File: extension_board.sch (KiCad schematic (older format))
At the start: 37 parts, among them CN1 Conn_02x20_Odd_Even, CN11 Conn_02x05_Odd_Even, CN12 Conn_02x20_Odd_Even, J1 Screw_Terminal_01x02, J2 Conn_01x02, J3 Conn_01x02, J4 Conn_01x02, J5 Conn_02x03_Odd_Even, J6 Conn_01x02, J7 Conn_02x14_Odd_Even, U1 LM334Z, U2 LM334Z, U3 LM334Z, U4 LM334Z

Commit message: first version of the pcb
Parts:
- removed CN11: Conn_02x05_Odd_Even, symbol Connector_Generic:Conn_02x05_Odd_Even
- removed CN12: Conn_02x20_Odd_Even, symbol Connector_Generic:Conn_02x20_Odd_Even
- added J8: Conn_02x10_Odd_Even, Connector_PinHeader_2.54mm:PinHeader_2x10_P2.54mm_Vertical, symbol Connector_Generic:Conn_02x10_Odd_Even
- added J9: Conn_02x19_Odd_Even, Connector_PinHeader_2.54mm:PinHeader_2x19_P2.54mm_Vertical, symbol Connector_Generic:Conn_02x19_Odd_Even
- C1: footprint (none) -> Capacitor_SMD:CP_Elec_4x5.8
- CN1: footprint (none) -> Connector_PinHeader_2.54mm:PinHeader_2x20_P2.54mm_Vertical_SMD
- D1: footprint (none) -> LED_SMD:LED_0805_2012Metric_Pad1.15x1.40mm_HandSolder
- J1: footprint (none) -> digikey-footprints:Term_Block_1x2_P5.08MM
- J2, J3, J4, J6: footprint (none) -> Connector_PinHeader_2.54mm:PinHeader_2x01_P2.54mm_Vertical_SMD
- J5: footprint (none) -> Connector_PinHeader_2.54mm:PinHeader_2x03_P2.54mm_Vertical_SMD
- J7: footprint (none) -> Connector_PinHeader_2.54mm:PinHeader_2x14_P2.54mm_Vertical_SMD
- R1, R2, R3, R4, R5, R6, R7, R8, R9: footprint (none) -> Resistor_SMD:R_0805_2012Metric_Pad1.15x1.40mm_HandSolder
- RV1, RV2, RV3, RV4: footprint (none) -> digikey-footprints:Trimpot_3.8mmx3.6mm_TC33X-2-103E
- TP1, TP2, TP3, TP4: footprint (none) -> TestPoint:TestPoint_Pad_2.5x2.5mm
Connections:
- net labels added: PA15, PF7
- wire segments 111 -> 113
- no-connect marks 55 -> 59

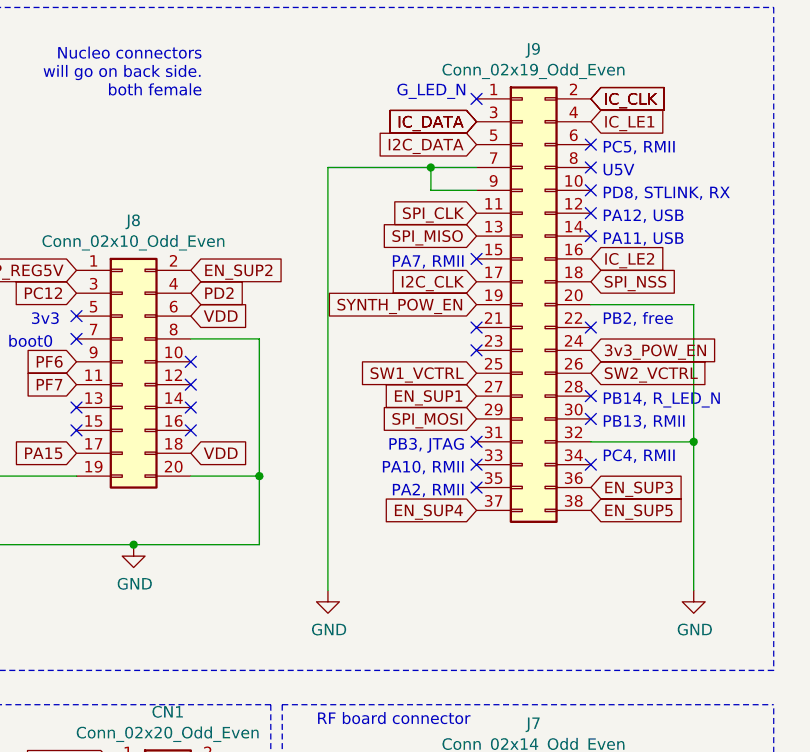
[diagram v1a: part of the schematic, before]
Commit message: had shorted gnd and AVDD on the cn12 connector
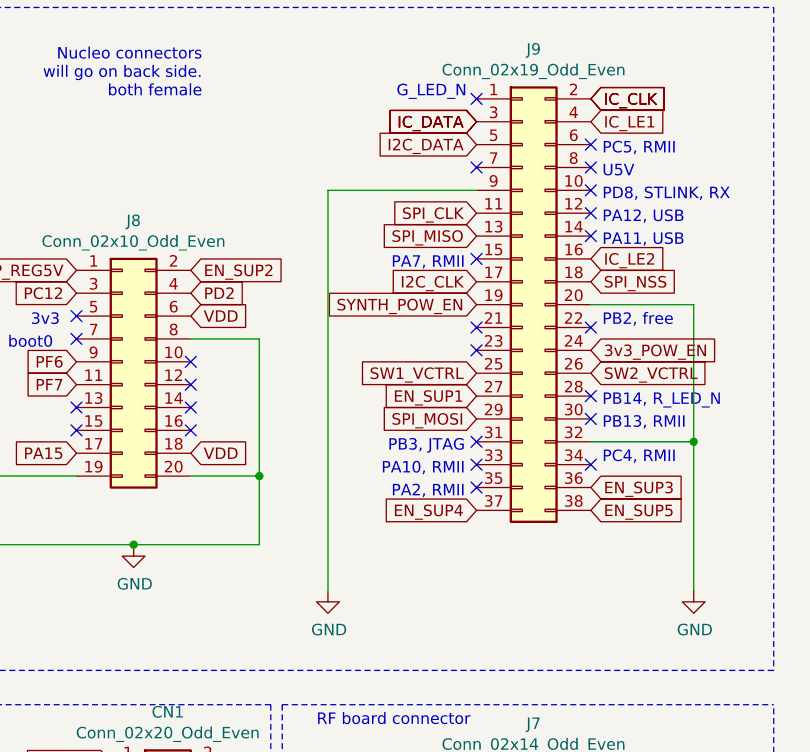
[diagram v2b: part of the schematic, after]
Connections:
- wire segments 113 -> 110
- no-connect marks 59 -> 60
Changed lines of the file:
@@
 Text Notes 7450 7500 0    50   ~ 0
 Glue board to connect to Nucleo, Power board and RF board
-Wire Wire Line
-	9800 1350 9600 1350
-Wire Wire Line
-	9600 1350 9600 1250
 $Comp
 L power:GND #PWR09
@@
 Text GLabel 9800 1850 0    50   Input ~ 0
 SYNTH_POW_EN
-Wire Wire Line
-	9150 1250 9600 1250
-Connection ~ 9600 1250
-Wire Wire Line
-	9600 1250 9800 1250
 Text GLabel 9800 1750 0    50   Input ~ 0
 I2C_CLK
@@
 	1    0    0    -1
 $EndComp
-Wire Wire Line
-	9150 1250 9150 3100
 NoConn ~ 8050 2300
 NoConn ~ 8050 2400
@@
 Wire Wire Line
 	5950 4800 5950 4900
+Wire Wire Line
+	9150 1350 9150 3100
+Wire Wire Line
+	9150 1350 9800 1350
+NoConn ~ 9800 1250
 $EndSCHEMATC

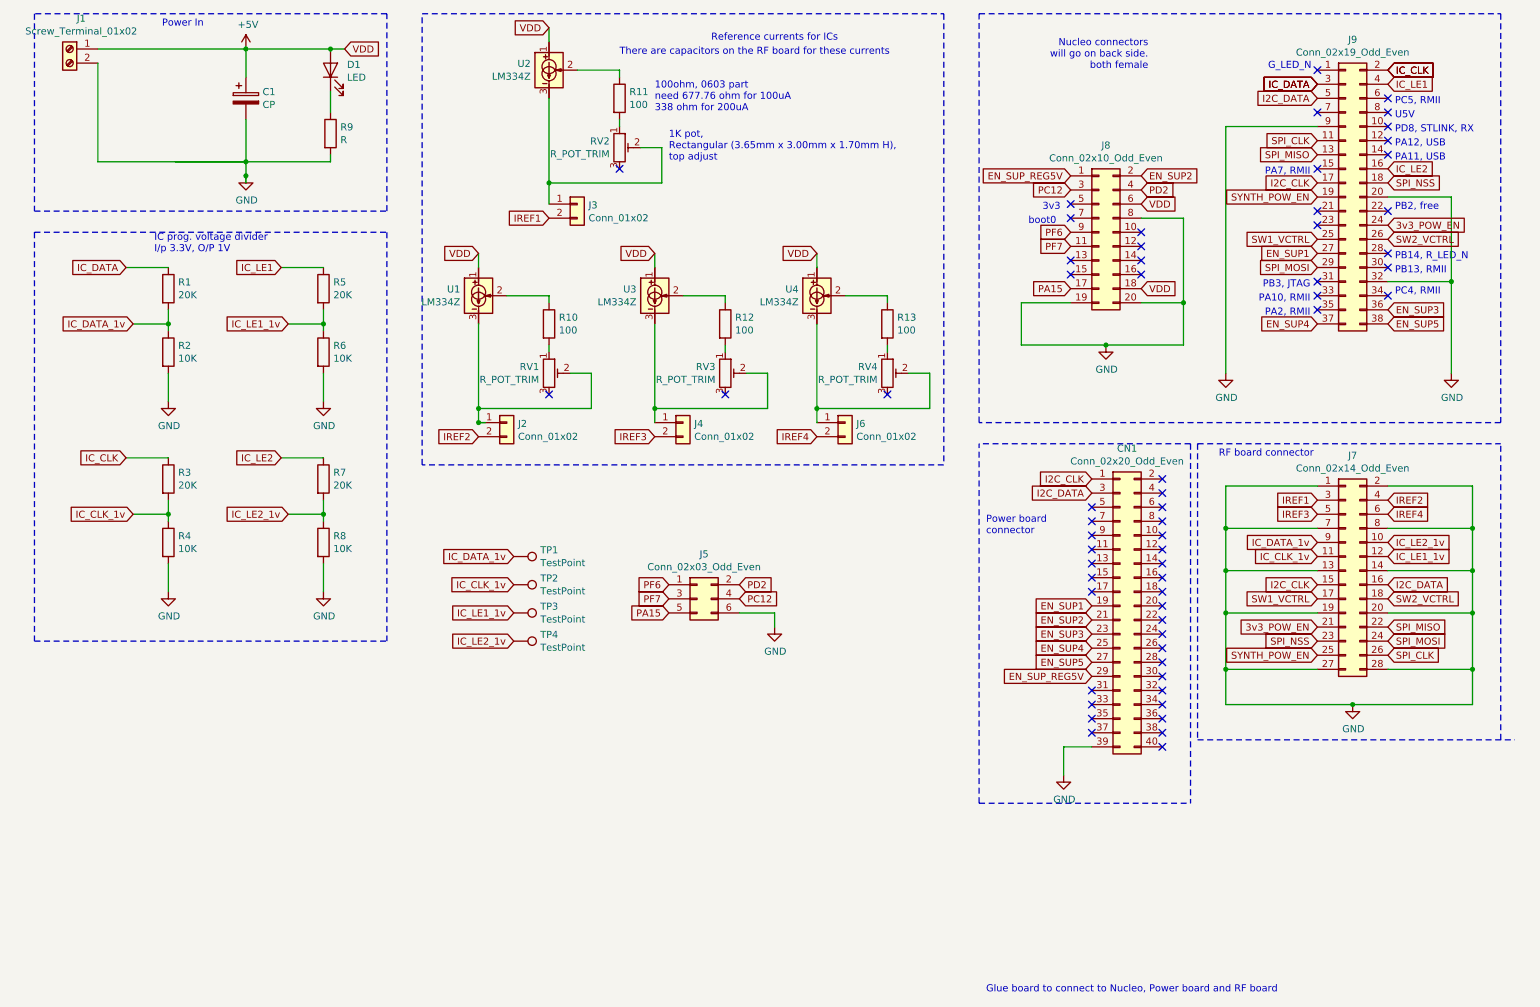
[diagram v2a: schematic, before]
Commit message: changed footprint assignments, added reset circuit
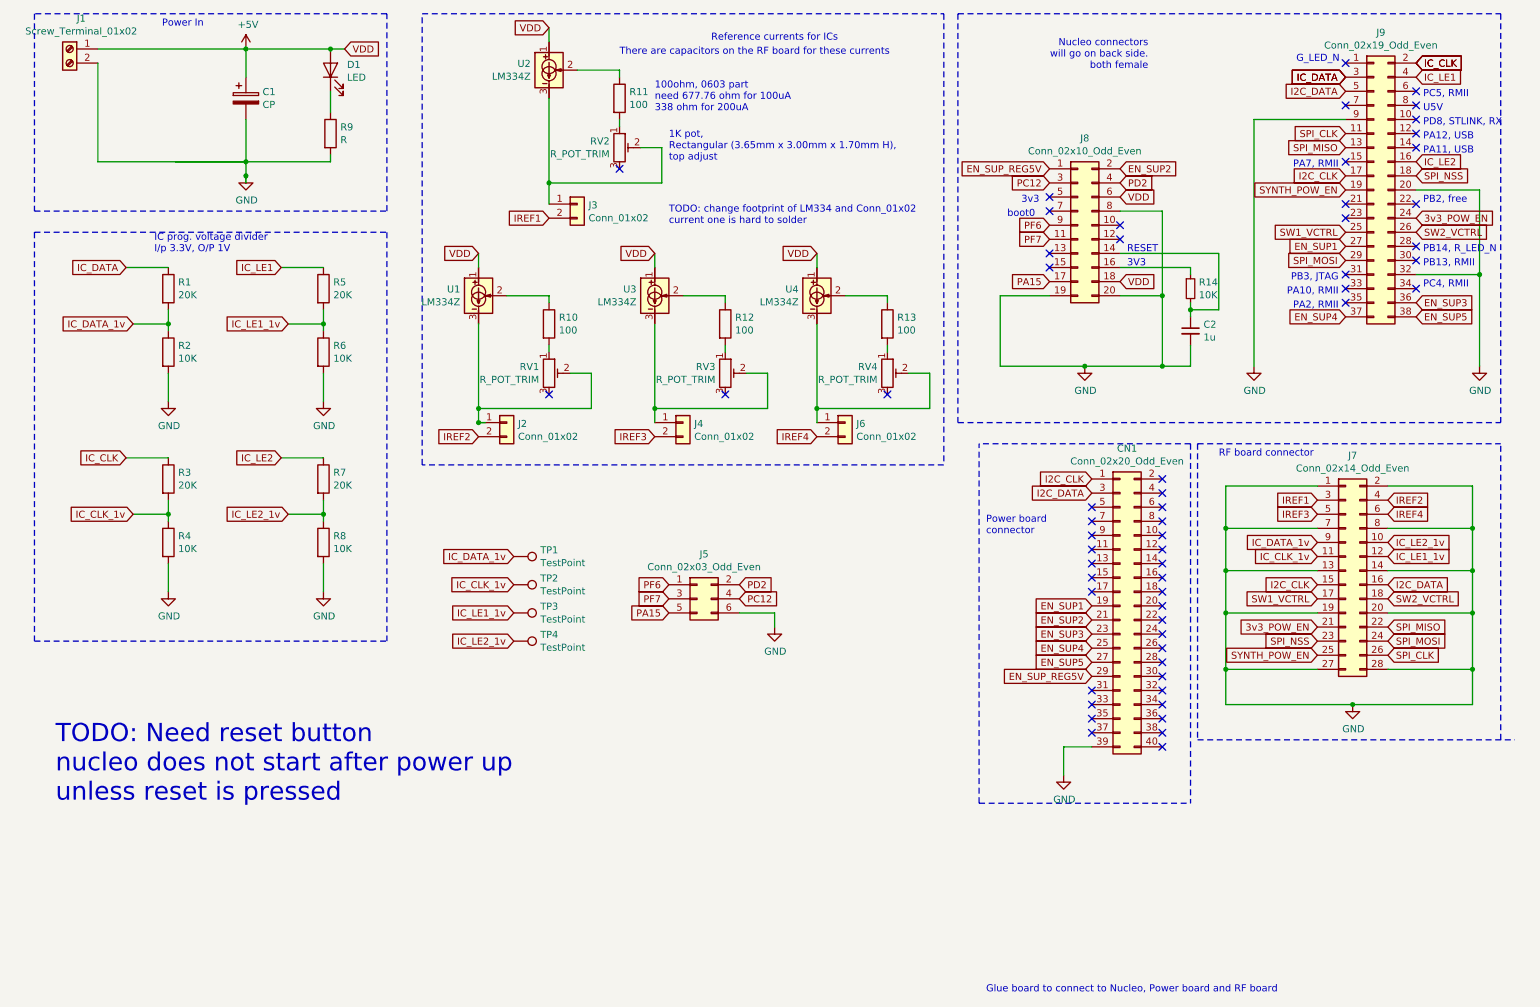
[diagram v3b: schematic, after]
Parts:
- added C2: 1u, Capacitor_SMD:C_0805_2012Metric_Pad1.15x1.40mm_HandSolder, symbol Device:C_Small
- added R14: 10K, Resistor_SMD:R_0805_2012Metric_Pad1.15x1.40mm_HandSolder, symbol Device:R_Small
- TP1, TP2, TP3, TP4: footprint TestPoint:TestPoint_Pad_2.5x2.5mm -> TestPoint:TestPoint_Pad_1.0x1.0mm
- U1, U2, U3, U4: footprint Package_TO_SOT_THT:TO-92_Inline -> Package_TO_SOT_THT:TO-92_Inline_Wide
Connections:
- wire segments 110 -> 119
- no-connect marks 60 -> 58
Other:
- note added: "3V3"
- note added: "RESET"
- note added: "TODO: Need reset button\nnucleo does not start after power up \nunless reset is pressed"
- note added: "TODO: change footprint of LM334 and Conn_01x02\ncurrent one is hard to solder"
- moved on the sheet: J8, J9

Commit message: gerber files and final files
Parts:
- removed CN1: Conn_02x20_Odd_Even, Connector_PinHeader_2.54mm:PinHeader_2x20_P2.54mm_Vertical_SMD, symbol Connector_Generic:Conn_02x20_Odd_Even
- added J10: Conn_01x09_Male, Connector_PinHeader_2.54mm:PinHeader_1x09_P2.54mm_Vertical_SMD_Pin1Left, symbol Connector:Conn_01x09_Male
- J2, J3, J4, J6: footprint Connector_PinHeader_2.54mm:PinHeader_2x01_P2.54mm_Vertical_SMD -> Connector_PinHeader_2.54mm:PinHeader_1x02_P2.54mm_Vertical
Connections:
- net EN_SUP1: now also J10.3 (Pin_3)
- net EN_SUP2: now also J10.4 (Pin_4)
- net EN_SUP3: now also J10.5 (Pin_5)
- net EN_SUP4: now also J10.6 (Pin_6)
- net EN_SUP5: now also J10.7 (Pin_7)
- net EN_SUP_REG5V: now also J10.8 (Pin_8)
- net GND: now also J10.9 (Pin_9)
- net I2C_CLK: now also J10.1 (Pin_1)
- net I2C_DATA: now also J10.2 (Pin_2)
- no-connect marks 58 -> 27
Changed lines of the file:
@@
 1K pot, \nRectangular (3.65mm x 3.00mm x 1.70mm H), \ntop adjust\n
 NoConn ~ 4850 1650
-$Comp
-L Connector_Generic:Conn_02x20_Odd_Even CN1
-U 1 1 6052AEFD
-P 8400 4750
-F 0 "CN1" H 8450 5867 50  0000 C CNN
-F 1 "Conn_02x20_Odd_Even" H 8450 5776 50  0000 C CNN
-F 2 "Connector_PinHeader_2.54mm:PinHeader_2x20_P2.54mm_Vertical_SMD" H 8400 4750 50  0001 C CNN
-F 3 "~" H 8400 4750 50  0001 C CNN
-	1    8400 4750
-	1    0    0    -1
-$EndComp
 Text GLabel 8200 3950 0    50   Input ~ 0
 I2C_DATA
 Text GLabel 8200 3850 0    50   Input ~ 0
 I2C_CLK
-NoConn ~ 8200 4050
-NoConn ~ 8200 4150
-NoConn ~ 8200 4250
-NoConn ~ 8200 4350
-NoConn ~ 8200 4450
-NoConn ~ 8200 4550
-NoConn ~ 8200 4650
-Text GLabel 8200 4750 0    50   Input ~ 0
+Text GLabel 8200 4050 0    50   Input ~ 0
 EN_SUP1
-Text GLabel 8200 4850 0    50   Input ~ 0
+Text GLabel 8200 4150 0    50   Input ~ 0
 EN_SUP2
-Text GLabel 8200 4950 0    50   Input ~ 0
+Text GLabel 8200 4250 0    50   Input ~ 0
 EN_SUP3
-Text GLabel 8200 5050 0    50   Input ~ 0
+Text GLabel 8200 4350 0    50   Input ~ 0
 EN_SUP4
-Text GLabel 8200 5150 0    50   Input ~ 0
+Text GLabel 8200 4450 0    50   Input ~ 0
 EN_SUP5
-Text GLabel 8200 5250 0    50   Input ~ 0
+Text GLabel 8200 4550 0    50   Input ~ 0
 EN_SUP_REG5V
-NoConn ~ 8200 5350
-NoConn ~ 8200 5450
-NoConn ~ 8200 5550
-NoConn ~ 8200 5650
-Wire Wire Line
-	8000 5750 8000 5950
-Wire Wire Line
-	8000 5750 8200 5750
+Wire Wire Line
+	8000 4650 8000 4850
 $Comp
 L power:GND #PWR08
 U 1 1 60545C1E
-P 8000 5950
-F 0 "#PWR08" H 8000 5700 50  0001 C CNN
-F 1 "GND" H 8005 5777 50  0000 C CNN
-F 2 "" H 8000 5950 50  0001 C CNN
-F 3 "" H 8000 5950 50  0001 C CNN
-	1    8000 5950
-	1    0    0    -1
-$EndComp
-NoConn ~ 8700 3850
-NoConn ~ 8700 3950
-NoConn ~ 8700 4050
-NoConn ~ 8700 4150
-NoConn ~ 8700 4250
-NoConn ~ 8700 4350
-NoConn ~ 8700 4450
-NoConn ~ 8700 4550
-NoConn ~ 8700 4650
-NoConn ~ 8700 4750
-NoConn ~ 8700 4850
-NoConn ~ 8700 4950
-NoConn ~ 8700 5050
-NoConn ~ 8700 5150
-NoConn ~ 8700 5250
-NoConn ~ 8700 5350
-NoConn ~ 8700 5450
-NoConn ~ 8700 5550
-NoConn ~ 8700 5650
-NoConn ~ 8700 5750
+P 8000 4850
+F 0 "#PWR08" H 8000 4600 50  0001 C CNN
+F 1 "GND" H 8005 4677 50  0000 C CNN
+F 2 "" H 8000 4850 50  0001 C CNN
+F 3 "" H 8000 4850 50  0001 C CNN
+	1    8000 4850
+	1    0    0    -1
+$EndComp
 Connection ~ 4350 1750
 Wire Wire Line
@@
 Wire Wire Line
 	4350 750  4350 650
-Wire Notes Line
-	8900 3600 8900 6150
-Wire Notes Line
-	7400 6150 7400 3600
 Text Notes 7450 4250 0    50   ~ 0
 Power board \nconnector
@@
 Wire Notes Line
 	8950 3600 11100 3600
-Wire Notes Line
-	7400 6150 8900 6150
 Text GLabel 3850 2250 0    50   Input ~ 0
 VDD
@@
 F 0 "J3" H 4630 1892 50  0000 L CNN
 F 1 "Conn_01x02" H 4630 1801 50  0000 L CNN
-F 2 "Connector_PinHeader_2.54mm:PinHeader_2x01_P2.54mm_Vertical_SMD" H 4550 1900 50  0001 C CNN
+F 2 "Connector_PinHeader_2.54mm:PinHeader_1x02_P2.54mm_Vertical" H 4550 1900 50  0001 C CNN
 F 3 "~" H 4550 1900 50  0001 C CNN
 	1    4550 1900
@@
 F 0 "J2" H 4130 3442 50  0000 L CNN
 F 1 "Conn_01x02" H 4130 3351 50  0000 L CNN
-F 2 "Connector_PinHeader_2.54mm:PinHeader_2x01_P2.54mm_Vertical_SMD" H 4050 3450 50  0001 C CNN
+F 2 "Connector_PinHeader_2.54mm:PinHeader_1x02_P2.54mm_Vertical" H 4050 3450 50  0001 C CNN
 F 3 "~" H 4050 3450 50  0001 C CNN
 	1    4050 3450
@@
 F 0 "J4" H 5380 3442 50  0000 L CNN
 F 1 "Conn_01x02" H 5380 3351 50  0000 L CNN
-F 2 "Connector_PinHeader_2.54mm:PinHeader_2x01_P2.54mm_Vertical_SMD" H 5300 3450 50  0001 C CNN
+F 2 "Connector_PinHeader_2.54mm:PinHeader_1x02_P2.54mm_Vertical" H 5300 3450 50  0001 C CNN
 F 3 "~" H 5300 3450 50  0001 C CNN
 	1    5300 3450
@@
 F 0 "J6" H 6530 3442 50  0000 L CNN
 F 1 "Conn_01x02" H 6530 3351 50  0000 L CNN
-F 2 "Connector_PinHeader_2.54mm:PinHeader_2x01_P2.54mm_Vertical_SMD" H 6450 3450 50  0001 C CNN
+F 2 "Connector_PinHeader_2.54mm:PinHeader_1x02_P2.54mm_Vertical" H 6450 3450 50  0001 C CNN
 F 3 "~" H 6450 3450 50  0001 C CNN
 	1    6450 3450
@@
 	8900 2600 8900 2650
 Connection ~ 8900 2650
+$Comp
+L Connector:Conn_01x09_Male J10
+U 1 1 60D91420
+P 8550 4250
+F 0 "J10" H 8522 4274 50  0000 R CNN
+F 1 "Conn_01x09_Male" H 8522 4183 50  0000 R CNN
+F 2 "Connector_PinHeader_2.54mm:PinHeader_1x09_P2.54mm_Vertical_SMD_Pin1Left" H 8550 4250 50  0001 C CNN
+F 3 "~" H 8550 4250 50  0001 C CNN
+	1    8550 4250
+	-1   0    0    -1
+$EndComp
+Wire Wire Line
+	8200 3850 8350 3850
+Wire Wire Line
+	8350 3950 8200 3950
+Wire Wire Line
+	8200 4050 8350 4050
+Wire Wire Line
+	8200 4150 8350 4150
+Wire Wire Line
+	8200 4250 8350 4250
+Wire Wire Line
+	8200 4350 8350 4350
+Wire Wire Line
+	8200 4450 8350 4450
+Wire Wire Line
+	8200 4550 8350 4550
+Wire Wire Line
+	8000 4650 8350 4650
+Wire Notes Line
+	8900 3600 8900 5150
+Wire Notes Line
+	7400 5150 8900 5150
+Wire Notes Line
+	7400 5150 7400 3600
 $EndSCHEMATC
